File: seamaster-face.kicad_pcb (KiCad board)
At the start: 2 copper layers, 27.3 x 27.3 mm, 1 part

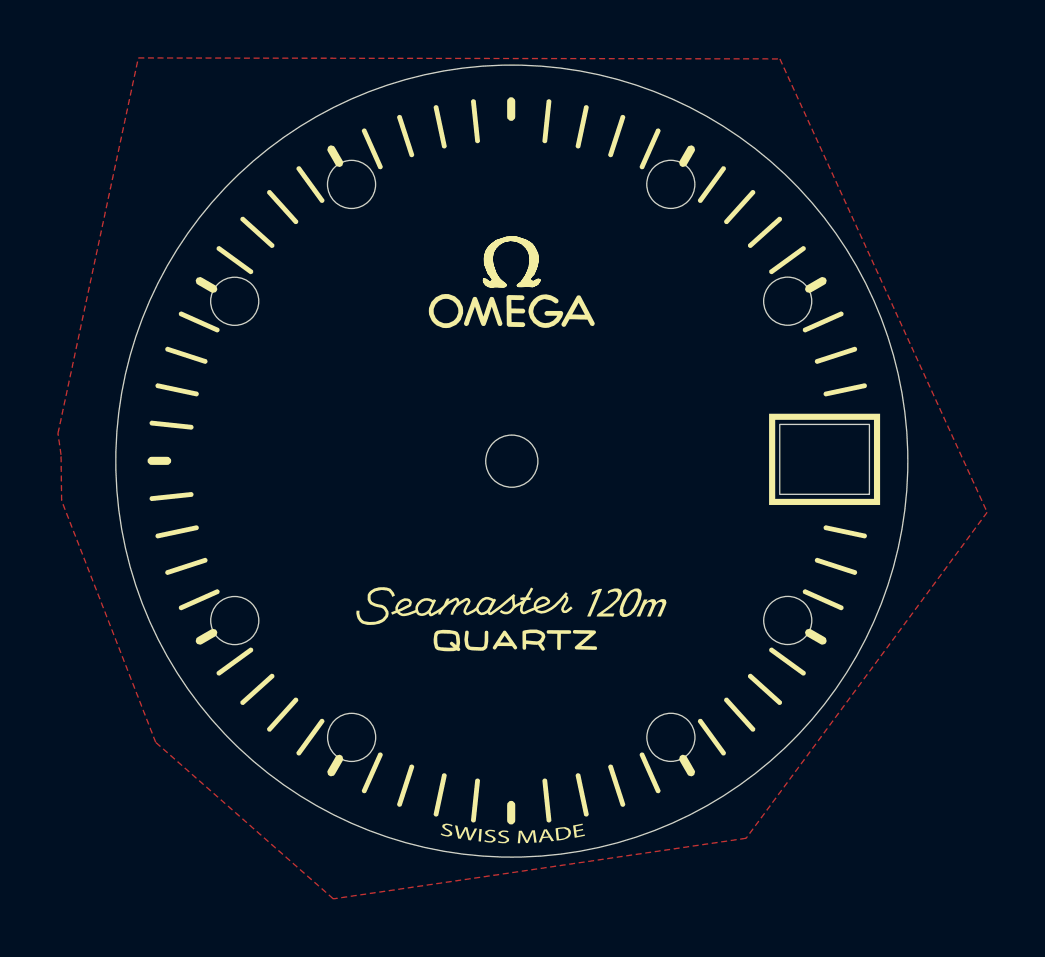
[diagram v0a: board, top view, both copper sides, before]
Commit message: add copper on back, add alignment guide on back, remove mfg mark guide
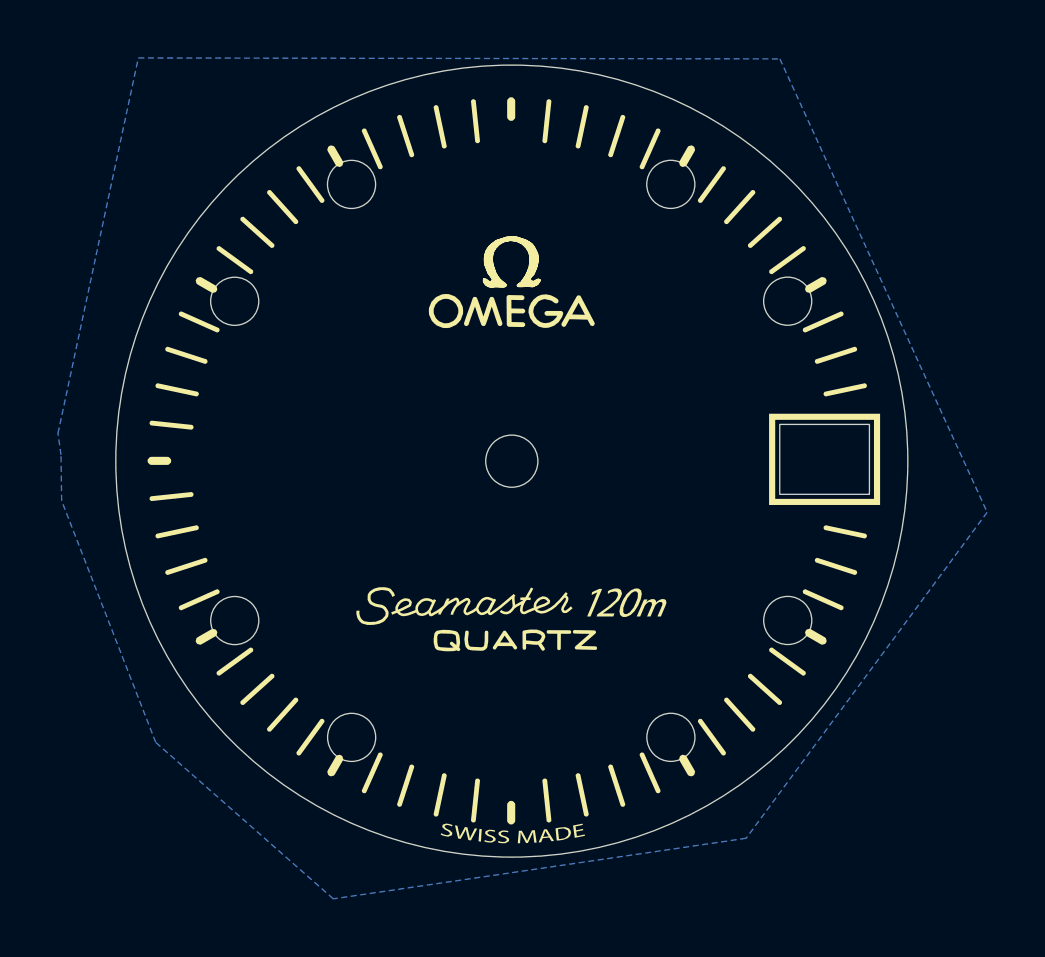
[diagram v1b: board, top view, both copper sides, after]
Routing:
- added copper zone on B.Cu, net (none)
- removed copper zone on F.Cu, net (none)
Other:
- net class Default: clearance 0.2 -> 0; trace_width 0.25 -> 0
- rule trace_clearance: 0.2 -> 0
- rule trace_min: 0.2 -> 0
- rule via_min_drill: 0.3 -> 0
- rule via_min_size: 0.4 -> 0
- board text removed: "ALLPCBALLPCBALLPCB"
